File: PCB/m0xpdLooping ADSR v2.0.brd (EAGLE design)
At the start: 107.6 x 38.1 mm, 69 parts, among them IC1 TL074P, IC2 7555, Q1 2N3904, Q2 2N3904, Q3 2N3904, Q5 2N3904, Q6 2N3904, Q7 2N3904, Q8 2N7000, SW1 TL46PO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

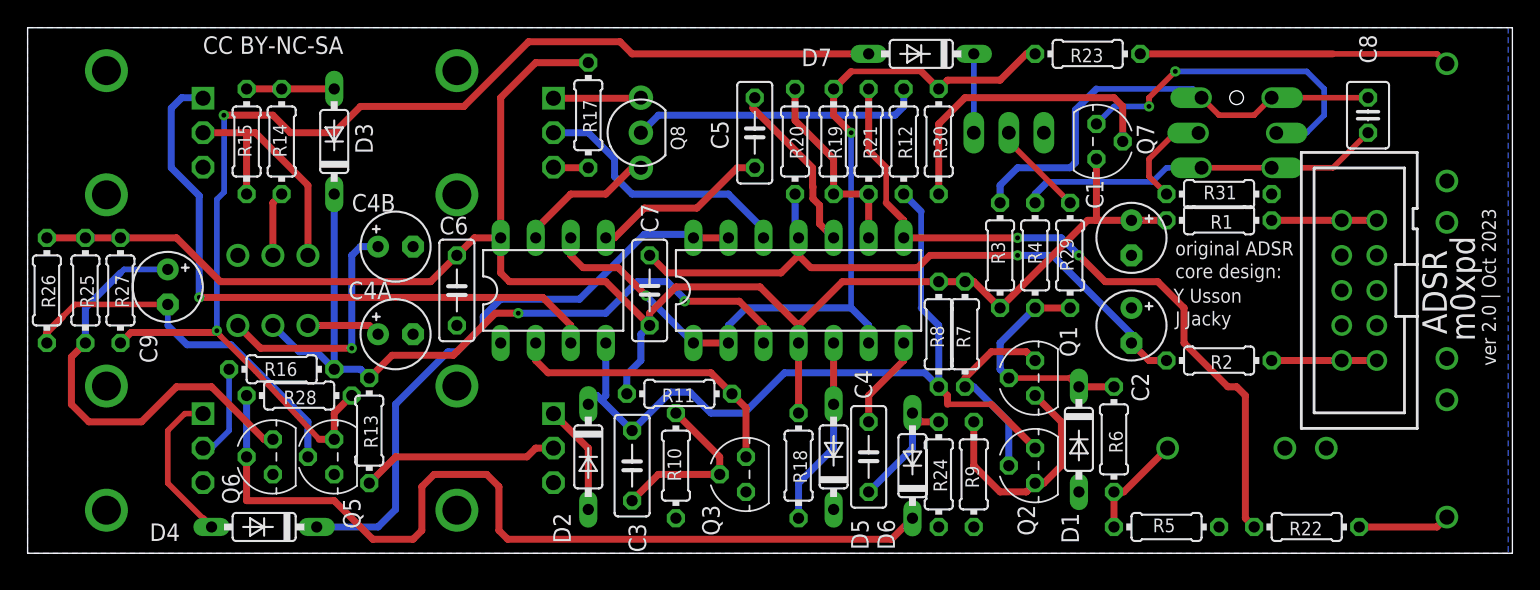
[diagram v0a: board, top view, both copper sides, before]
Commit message: PCB without vias
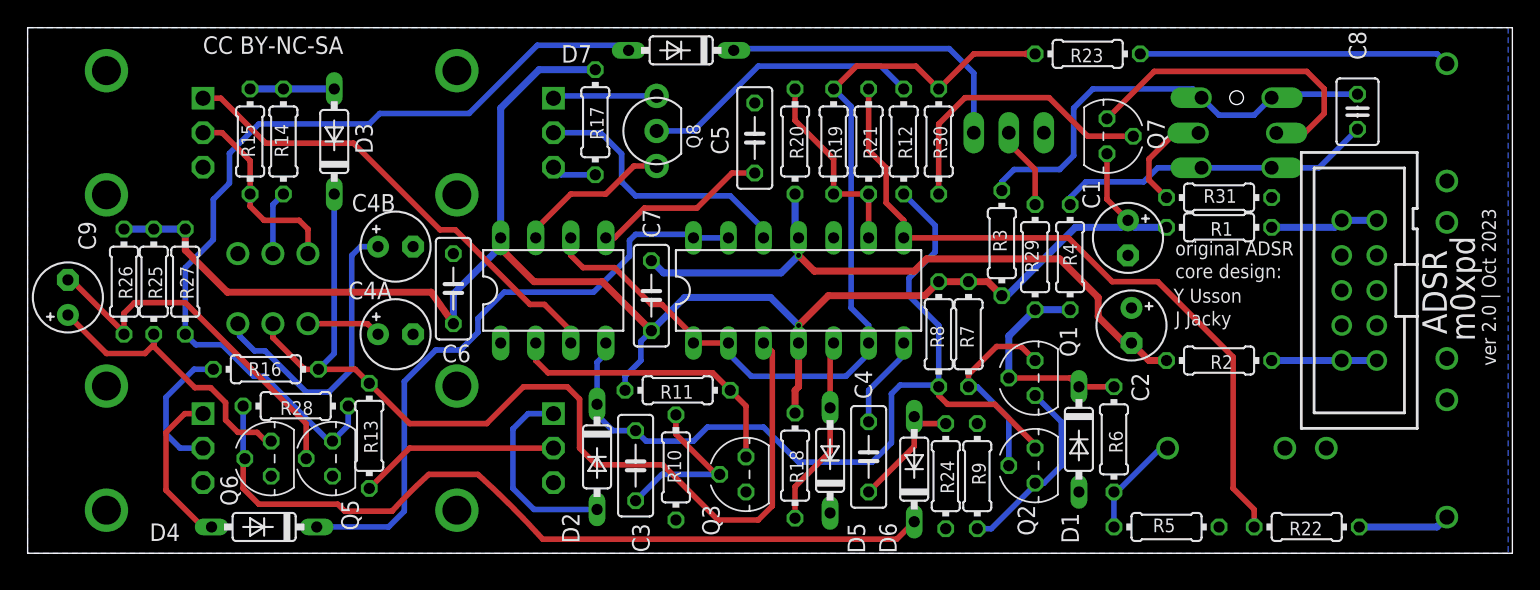
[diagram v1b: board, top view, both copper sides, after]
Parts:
- moved D7 17.4 mm to (47.4, 36.4)
- moved C9 7.28 mm to (2.92, 18.5), turned to 90 degrees
- moved R26 5.62 mm to (6.99, 19.7)
- moved R25 4.99 mm to (9.14, 19.7)
- moved R27 4.74 mm to (11.4, 19.7)
- moved R29 2.54 mm to (73.0, 21.5)
- moved R4 2.54 mm to (75.6, 21.5)
- moved Q8 1.15 mm to (45.6, 30.6)
- moved R16 1.14 mm to (17.3, 13.3)
- moved R3 0.90 mm to (70.6, 22.5)
- moved Q7 0.85 mm to (78.2, 30.2)
- moved C8 0.80 mm to (96.4, 32.0)
- moved R28 0.80 mm to (19.4, 10.7)
- moved R17 0.72 mm to (41.1, 31.2)
- moved D2 0.63 mm to (41.3, 6.99)
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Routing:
- net N$38: track 89.3 -> 63.7 mm, vias 2 -> 0
- net N$21: track 55.4 -> 72.6 mm, vias 2 -> 0
- net N$42: track 5.71 -> 22.5 mm
- net GND: track 12.6 -> 0.00 mm
- net N$6: track 46.2 -> 34.5 mm, vias 1 -> 0
- net N$39: track 32.3 -> 21.4 mm
- net N$14: track 8.01 -> 14.4 mm
- net N$43: track 65.3 -> 59.0 mm
- net N$18: track 18.7 -> 14.2 mm
- net N$11: track 58.6 -> 62.9 mm
- net N$24: track 17.8 -> 21.9 mm, vias 1 -> 0
- net N$36: track 26.6 -> 23.4 mm
- net N$22: track 6.86 -> 10.0 mm
- net N$4: track 17.0 -> 13.9 mm
- net N$25: track 62.2 -> 65.2 mm, vias 2 -> 0
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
